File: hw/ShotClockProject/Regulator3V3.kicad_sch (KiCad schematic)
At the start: 13 parts, among them U2 TPS63000

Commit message: Added LCSC Part number
Renamed output folders
Created first output files for REV1
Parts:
- C14: LCSC Part (none) -> C1525; LCSC Part # (none) -> C1525
- C15, C16, C17: LCSC Part (none) -> C96446; LCSC Part # (none) -> C96446
- C18: LCSC Part (none) -> C1559; LCSC Part # (none) -> C1559
- D2: LCSC Part (none) -> C72043; LCSC Part # (none) -> C72043
- L1: LCSC Part (none) -> C404494; LCSC Part # (none) -> C404494
- R10: LCSC Part (none) -> C25867; LCSC Part # (none) -> C25867
- R10: LCSC Part (none) -> C25076; LCSC Part # (none) -> C25076
- R11: LCSC Part (none) -> C144787; LCSC Part # (none) -> C144787
- R12: LCSC Part (none) -> C185459; LCSC Part # (none) -> C185459
- U2: LCSC Part (none) -> C24966; LCSC Part # (none) -> C24966
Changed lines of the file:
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@@
+      (effects (font (size 1.27 1.27)) hide)
+    )
+    (property "LCSC Part #" "C25867" (at 154.94 54.61 0)
+      (effects (font (size 1.27 1.27)) hide)
+    )
+    (property "LCSC Part" "C25867" (at 154.94 54.61 0)
       (effects (font (size 1.27 1.27)) hide)
     )
@@
     )
     (property "Datasheet" "~" (at 144.78 44.45 0)
+      (effects (font (size 1.27 1.27)) hide)
+    )
+    (property "LCSC Part #" "C96446" (at 144.78 44.45 0)
+      (effects (font (size 1.27 1.27)) hide)
+    )
+    (property "LCSC Part" "C96446" (at 144.78 44.45 0)
       (effects (font (size 1.27 1.27)) hide)
     )
@@
       (effects (font (size 1.27 1.27)) hide)
     )
+    (property "LCSC Part #" "C1525" (at 59.69 52.07 0)
+      (effects (font (size 1.27 1.27)) hide)
+    )
+    (property "LCSC Part" "C1525" (at 59.69 52.07 0)
+      (effects (font (size 1.27 1.27)) hide)
+    )
     (pin "1")
     (pin "2")
@@
       (effects (font (size 1.27 1.27)) hide)
     )
+    (property "LCSC Part #" "C144787" (at 102.87 41.91 0)
+      (effects (font (size 1.27 1.27)) hide)
+    )
+    (property "LCSC Part" "C144787" (at 102.87 41.91 0)
+      (effects (font (size 1.27 1.27)) hide)
+    )
     (pin "1")
     (pin "2")
@@
       (effects (font (size 1.27 1.27)) hide)
     )
+    (property "LCSC Part #" "C96446" (at 48.26 52.07 0)
+      (effects (font (size 1.27 1.27)) hide)
+    )
+    (property "LCSC Part" "C96446" (at 48.26 52.07 0)
+      (effects (font (size 1.27 1.27)) hide)
+    )
     (pin "1")
     (pin "2")
@@
     )
     (property "Datasheet" "http://www.ti.com/lit/ds/symlink/tps63000.pdf" (at 78.74 34.29 0)
+      (effects (font (size 1.27 1.27)) hide)
+    )
+    (property "LCSC Part #" "C24966" (at 86.36 48.26 0)
+      (effects (font (size 1.27 1.27)) hide)
+    )
+    (property "LCSC Part" "C24966" (at 86.36 48.26 0)
       (effects (font (size 1.27 1.27)) hide)
     )
@@
       (effects (font (size 1.27 1.27)) hide)
     )
+    (property "LCSC Part #" "C72043" (at 154.94 45.72 0)
+      (effects (font (size 1.27 1.27)) hide)
+    )
+    (property "LCSC Part" "C72043" (at 154.94 45.72 0)
+      (effects (font (size 1.27 1.27)) hide)
+    )
     (pin "1")
     (pin "2")
@@
       (effects (font (size 1.27 1.27)) hide)
     )
+    (property "LCSC Part #" "C96446" (at 134.62 44.45 0)
+      (effects (font (size 1.27 1.27)) hide)
+    )
+    (property "LCSC Part" "C96446" (at 134.62 44.45 0)
+      (effects (font (size 1.27 1.27)) hide)
+    )
     (pin "1")
     (pin "2")
@@
     )
     (property "Datasheet" "~" (at 102.87 49.53 0)
+      (effects (font (size 1.27 1.27)) hide)
+    )
+    (property "LCSC Part #" "C185459" (at 102.87 49.53 0)
+      (effects (font (size 1.27 1.27)) hide)
+    )
+    (property "LCSC Part" "C185459" (at 102.87 49.53 0)
       (effects (font (size 1.27 1.27)) hide)
     )
@@
       (effects (font (size 1.27 1.27)) hide)
     )
+    (property "LCSC Part #" "" (at 76.2 67.31 0)
+      (effects (font (size 1.27 1.27)) hide)
+    )
+    (property "LCSC Part" "" (at 76.2 67.31 0)
+      (effects (font (size 1.27 1.27)) hide)
+    )
     (pin "1")
     (pin "2")
@@
       (effects (font (size 1.27 1.27)) hide)
     )
+    (property "LCSC Part #" "C1559" (at 113.03 41.91 0)
+      (effects (font (size 1.27 1.27)) hide)
+    )
+    (property "LCSC Part" "C1559" (at 113.03 41.91 0)
+      (effects (font (size 1.27 1.27)) hide)
+    )
     (pin "1")
     (pin "2")
@@
       (effects (font (size 1.27 1.27)) hide)
     )
+    (property "LCSC Part #" "C25076" (at 59.69 41.91 0)
+      (effects (font (size 1.27 1.27)) hide)
+    )
+    (property "LCSC Part" "C25076" (at 59.69 41.91 0)
+      (effects (font (size 1.27 1.27)) hide)
+    )
     (pin "1")
     (pin "2")
@@
       (effects (font (size 1.27 1.27)) hide)
     )
+    (property "LCSC Part #" "C404494" (at 73.66 53.34 0)
+      (effects (font (size 1.27 1.27)) hide)
+    )
+    (property "LCSC Part" "C404494" (at 73.66 53.34 0)
+      (effects (font (size 1.27 1.27)) hide)
+    )

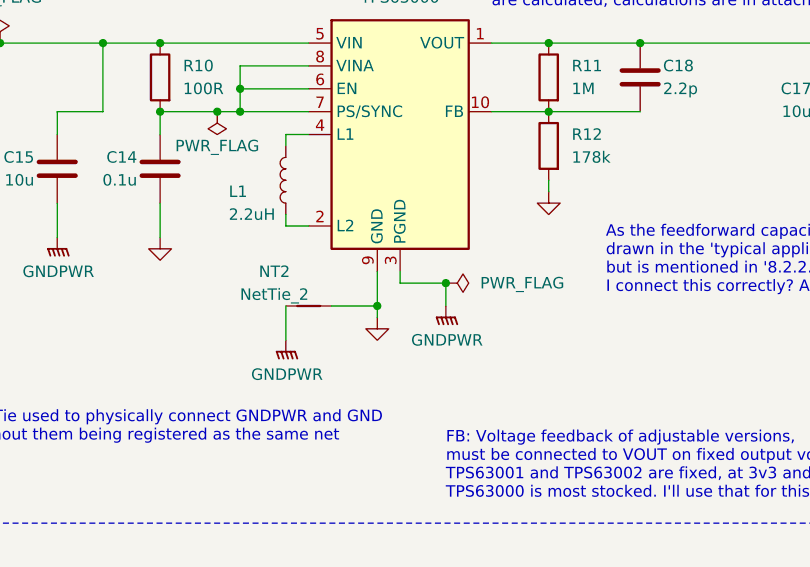
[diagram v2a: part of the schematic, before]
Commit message: Added LCSC part numbers, and changed TPS vias
- Changed the footprint for the TPS regulators, so they don't have 0.2mm vias. Manually placed GND vias next to the footprint.
- Removed NETTIES to get rid of weird across the map connection of GND and GNDPWR.
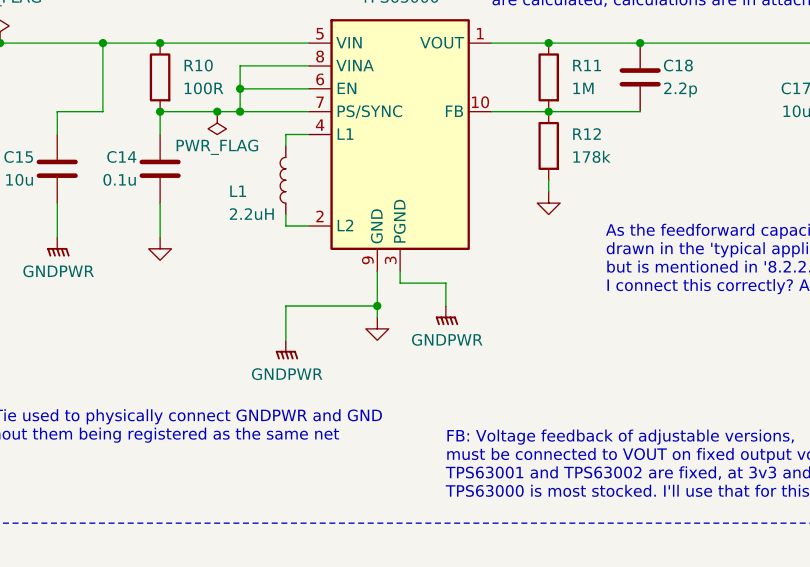
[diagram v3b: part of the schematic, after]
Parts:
- removed NT2: NetTie_2, NetTie:NetTie-2_SMD_Pad2.0mm, symbol Device:NetTie_2
- U2: footprint Package_SON_Altered:Texas_DRC0010J_ThermalVias_Altered -> Package_SON:Texas_DRC0010J
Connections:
- net GNDPWR is gone; now on net GND: C15.2, C16.2, C17.2, U2.11 (PGND), U2.3 (PGND)
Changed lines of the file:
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@@
   (junction (at 139.7 40.64) (diameter 0) (color 0 0 0 0)
   )
-  (junction (at 91.44 64.77) (diameter 0) (color 0 0 0 0)
-  )
   (wire (pts (xy 113.03 45.72) (xy 102.87 45.72))
     (stroke (width 0) (type default))
@@
     (stroke (width 0) (type default))
   )
-  (wire (pts (xy 78.74 67.31) (xy 83.82 67.31))
+  (wire (pts (xy 73.66 67.31) (xy 83.82 67.31))
     (stroke (width 0) (type default))
   )
@@
     )
   )
-  (symbol (lib_id "power:PWR_FLAG") (at 91.44 64.77 270) (unit 1)
-    (in_bom yes) (on_board yes) (dnp no) (fields_autoplaced)
-    (property "Reference" "#FLG02" (at 93.345 64.77 0)
-      (effects (font (size 1.27 1.27)) hide)
-    )
-    (property "Value" "PWR_FLAG" (at 95.25 64.77 90)
-      (effects (font (size 1.27 1.27)) (justify left))
-    )
-    (property "Footprint" "" (at 91.44 64.77 0)
-      (effects (font (size 1.27 1.27)) hide)
-    )
-    (property "Datasheet" "~" (at 91.44 64.77 0)
-      (effects (font (size 1.27 1.27)) hide)
-    )
-    (pin "1")
-    (instances
-      (project "ShotClockProject"
-        (path "/5fd859aa-754d-49c2-9762-3f7ebe3bb64c/d53b1cd8-24cb-4dc0-9a02-0cd96c1f4291"
-          (reference "#FLG02") (unit 1)
-        )
-        (path "/5fd859aa-754d-49c2-9762-3f7ebe3bb64c/d287d155-1951-4d4f-8d6c-570f03bc79f5"
-          (reference "#FLG06") (unit 1)
-        )
-        (path "/5fd859aa-754d-49c2-9762-3f7ebe3bb64c/17367eb9-0f4d-4017-b1ca-d50430410a5d"
-          (reference "#FLG010") (unit 1)
-        )
-        (path "/5fd859aa-754d-49c2-9762-3f7ebe3bb64c/83d8d19c-1376-4688-800d-ae057ad1fe11"
-          (reference "#FLG012") (unit 1)
-        )
-      )
-    )
-  )
   (symbol (lib_id "Device:C") (at 59.69 52.07 0) (mirror y) (unit 1)
     (in_bom yes) (on_board yes) (dnp no)
@@
       (effects (font (size 1.27 1.27)))
     )
-    (property "Footprint" "Package_SON_Altered:Texas_DRC0010J_ThermalVias_Altered" (at 107.95 62.23 0)
+    (property "Footprint" "Package_SON:Texas_DRC0010J" (at 107.95 62.23 0)
       (effects (font (size 1.27 1.27)) hide)
     )
@@
         )
       )
-    )
-  )
-  (symbol (lib_id "Device:NetTie_2") (at 76.2 67.31 0) (unit 1)
-    (in_bom no) (on_board yes) (dnp no)
-    (property "Reference" "NT2" (at 72.39 63.5 0)
-      (effects (font (size 1.27 1.27)))
-    )
-    (property "Value" "NetTie_2" (at 72.39 66.04 0)
-      (effects (font (size 1.27 1.27)))
-    )
-    (property "Footprint" "NetTie:NetTie-2_SMD_Pad2.0mm" (at 76.2 67.31 0)
-      (effects (font (size 1.27 1.27)) hide)
-    )
-    (property "Datasheet" "~" (at 76.2 67.31 0)
-      (effects (font (size 1.27 1.27)) hide)
-    )
-    (property "LCSC Part #" "" (at 76.2 67.31 0)
-      (effects (font (size 1.27 1.27)) hide)
-    )
-    (property "LCSC Part" "" (at 76.2 67.31 0)
-      (effects (font (size 1.27 1.27)) hide)
-    )
-    (pin "1")
-    (pin "2")
-    (instances
-      (project "ShotClockProject"
-        (path "/5fd859aa-754d-49c2-9762-3f7ebe3bb64c/17367eb9-0f4d-4017-b1ca-d50430410a5d"
-          (reference "NT2") (unit 1)
-        )
-        (path "/5fd859aa-754d-49c2-9762-3f7ebe3bb64c/83d8d19c-1376-4688-800d-ae057ad1fe11"
-          (reference "NT3") (unit 1)
-        )
-      )

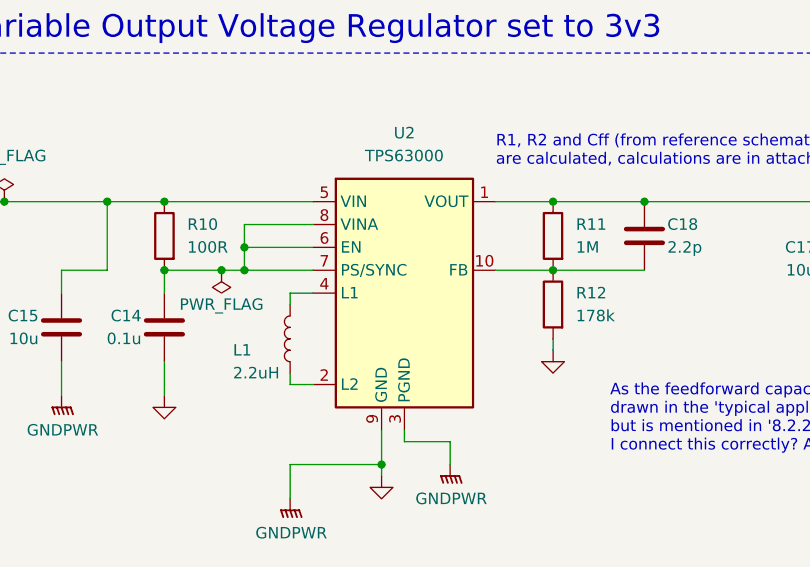
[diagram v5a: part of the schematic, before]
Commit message: Routed V regulators on mainboard
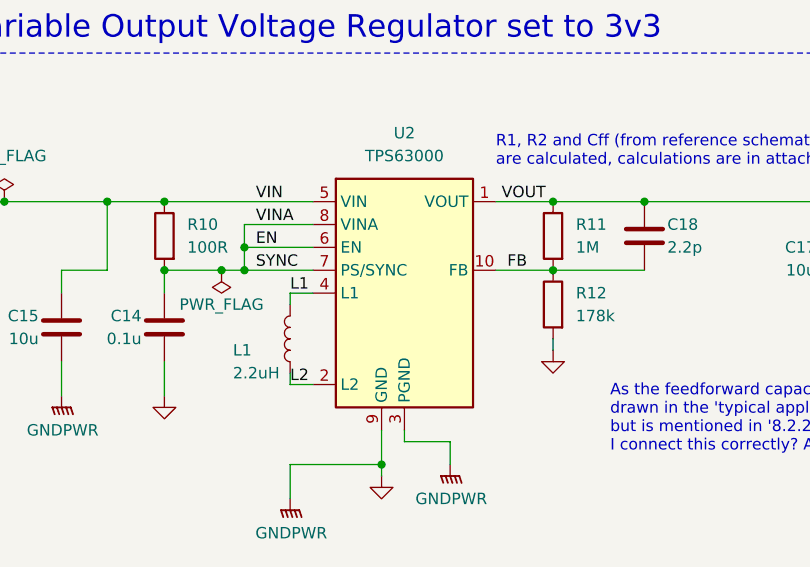
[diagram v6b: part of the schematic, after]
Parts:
- U2: footprint Package_SON:Texas_DRC0010J -> Package_SON_Altered:Texas_DRC0010J_Altered
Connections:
- net EN: now reaches C14.1, R10.2, U2.6 (EN), U2.7 (PS/SYNC), U2.8 (VINA)
- net FB: now reaches C18.2, R11.2, R12.1, U2.10 (FB)
- net L2: now reaches L1.2, U2.2 (L2)
- net L1: now reaches L1.1, U2.4 (L1)
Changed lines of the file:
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@@
     (effects (font (size 2.5 2.5) (color 255 0 0 1)) (justify left bottom))
+  )
+  (label "VOUT" (at 97.155 38.1 0) (fields_autoplaced)
+    (effects (font (size 1.27 1.27)) (justify left bottom))
+  )
+  (label "VIN" (at 69.85 38.1 0) (fields_autoplaced)
+    (effects (font (size 1.27 1.27)) (justify left bottom))
+  )
+  (label "VINA" (at 69.85 40.64 0) (fields_autoplaced)
+    (effects (font (size 1.27 1.27)) (justify left bottom))
+  )
+  (label "FB" (at 97.79 45.72 0) (fields_autoplaced)
+    (effects (font (size 1.27 1.27)) (justify left bottom))
+  )
+  (label "L2" (at 73.66 58.42 0) (fields_autoplaced)
+    (effects (font (size 1.27 1.27)) (justify left bottom))
+  )
+  (label "EN" (at 69.85 43.18 0) (fields_autoplaced)
+    (effects (font (size 1.27 1.27)) (justify left bottom))
+  )
+  (label "SYNC" (at 69.85 45.72 0) (fields_autoplaced)
+    (effects (font (size 1.27 1.27)) (justify left bottom))
+  )
+  (label "L1" (at 73.66 48.26 0) (fields_autoplaced)
+    (effects (font (size 1.27 1.27)) (justify left bottom))
   )
   (hierarchical_label "3v3_out" (shape output) (at 172.72 38.1 0) (fields_autoplaced)
@@
       (effects (font (size 1.27 1.27)))
     )
-    (property "Footprint" "Package_SON:Texas_DRC0010J" (at 107.95 62.23 0)
-      (effects (font (size 1.27 1.27)) hide)
-    )
+    (property "Footprint" "Package_SON_Altered:Texas_DRC0010J_Altered" (at 107.95 62.23 0)
+      (effects (font (size 1.27 1.27)) hide)
+    )
